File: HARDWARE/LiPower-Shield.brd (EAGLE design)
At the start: 59.7 x 53.3 mm, 51 parts, among them U1 MAX17043G+U, U2 TPS61200, U3 MCP73831, U4 ARDUINO_R3_SHIELD, X1 USBSMD

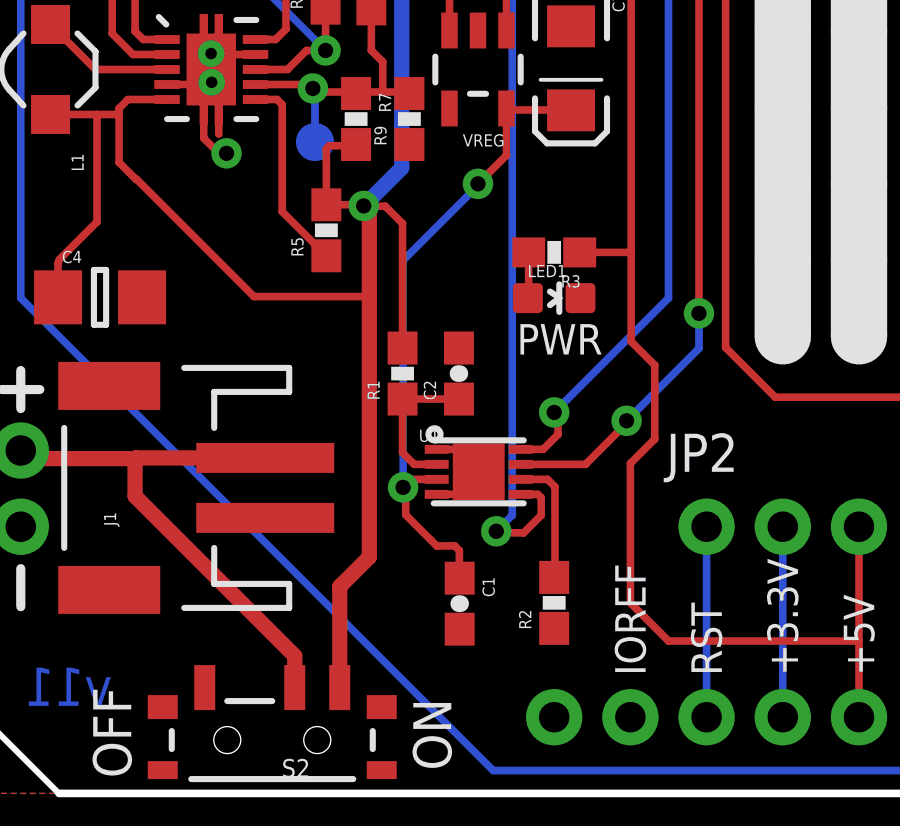
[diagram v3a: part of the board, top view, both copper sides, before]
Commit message: Added test point, Lines around Sch parts and Prod Att
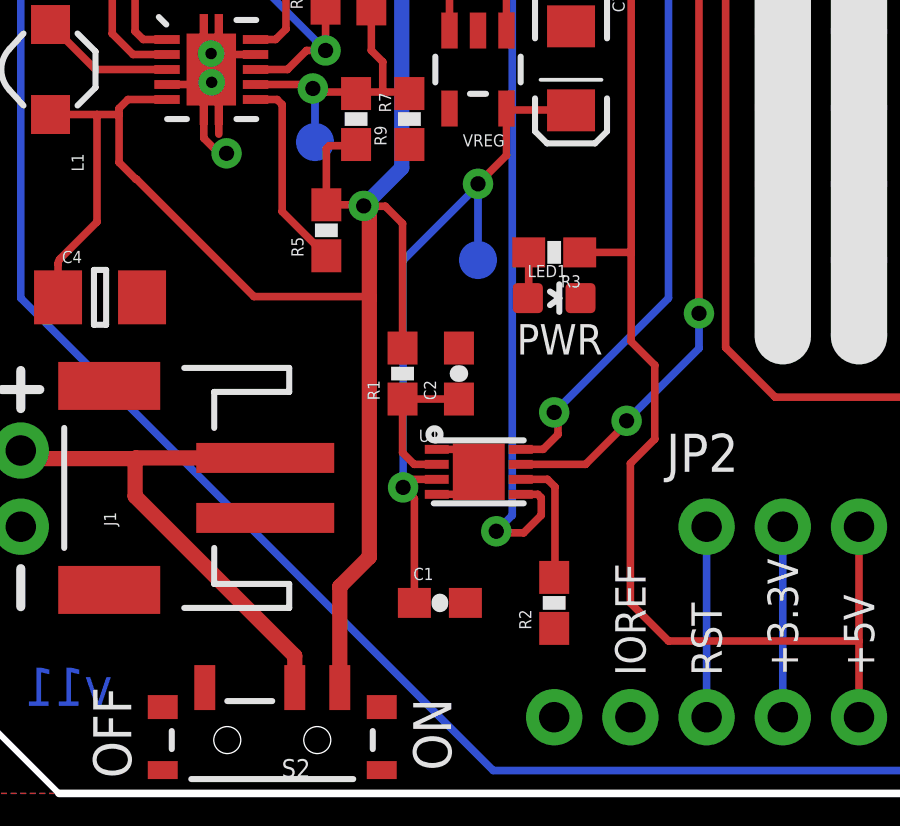
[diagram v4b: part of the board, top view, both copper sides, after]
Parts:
- removed U$2, U$3: (no value), SparkFun-Electromechanical:STAND-OFF-TIGHT
- added JP10, JP9: STAND-OFFTIGHT, SparkFun:STAND-OFF-TIGHT
- added TP2: TEST-POINT3X5, SparkFun-Passives:PAD.03X.05
- C7: device SparkFun:EIA3216 -> SparkFun-Capacitors:EIA3216
- U3, VREG: device SparkFun:SOT23-5 -> SparkFun-PowerIC:SOT23-5
- moved C1 0.66 mm to (15.2, 6.35), turned to 0 degrees
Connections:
- net 3.3V: now also TP2.P$1
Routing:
- net 3.3V: track 21.7 -> 24.5 mm
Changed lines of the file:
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@@
 <layer number="29" name="tStop" color="7" fill="3" visible="no" active="yes"/>
 <layer number="30" name="bStop" color="7" fill="6" visible="no" active="yes"/>
-<layer number="31" name="tCream" color="7" fill="4" visible="no" active="yes"/>
+<layer number="31" name="tCream" color="7" fill="4" visible="yes" active="yes"/>
 <layer number="32" name="bCream" color="7" fill="5" visible="no" active="yes"/>
 <layer number="33" name="tFinish" color="6" fill="3" visible="no" active="yes"/>
@@
 <element name="U4" library="SparkFun-Boards" package="UNO_R3_SHIELD" value="ARDUINO_R3_SHIELD" x="0" y="53.34" rot="R270"/>
 <element name="U1" library="SparkFun" package="TDFN-8" value="MAX17043G+U" x="16.5354" y="10.7188"/>
-<element name="C1" library="SparkFun-Capacitors" package="0603-CAP" value="10nF" x="15.9004" y="6.3246" rot="R270">
-<attribute name="PROD_ID" value="CAP-00867" x="15.9004" y="6.3246" size="1.778" layer="27" rot="R270" display="off"/>
-<attribute name="VALUE" value="10nF" x="15.9004" y="6.3246" size="1.778" layer="27" rot="R270" display="off"/>
-</element>
-<element name="U3" library="SparkFun" package="SOT23-5" value="MCP73831" x="13.97" y="38.1" rot="R90"/>
+<element name="C1" library="SparkFun-Capacitors" package="0603-CAP" value="10nF" x="15.24" y="6.35">
+<attribute name="PROD_ID" value="CAP-00867" x="15.24" y="6.35" size="1.778" layer="27" display="off"/>
+<attribute name="VALUE" value="10nF" x="15.24" y="6.35" size="1.778" layer="27" display="off"/>
+</element>
+<element name="U3" library="SparkFun-PowerIC" package="SOT23-5" value="MCP73831" x="13.97" y="38.1" rot="R90">
+<attribute name="PROD_ID" value="IC-09995" x="13.97" y="38.1" size="1.778" layer="27" rot="R90" display="off"/>
+</element>
 <element name="X1" library="SparkFun-Connectors" package="USB-MINIB" value="USBSMD" x="5.08" y="38.1">
 <attribute name="PROD_ID" value="CONN-08193" x="5.08" y="38.1" size="1.778" layer="27" display="off"/>
@@
 </element>
 <element name="JP4" library="SparkFun-Connectors" package="1X02" value="M02PTH" x="5.953759375" y="45.72" rot="R180"/>
-<element name="VREG" library="SparkFun" package="SOT23-5" value="MIC5205-3.3V" x="16.51" y="24.13" rot="R180"/>
-<element name="C7" library="SparkFun" package="EIA3216" value="10uF" x="19.611340625" y="24.1681" rot="R270"/>
+<element name="VREG" library="SparkFun-PowerIC" package="SOT23-5" value="MIC5205-3.3V" x="16.51" y="24.13" rot="R180">
+<attribute name="PROD_ID" value="VREG-00822" x="16.51" y="24.13" size="1.778" layer="27" rot="R180" display="off"/>
+</element>
+<element name="C7" library="SparkFun-Capacitors" package="EIA3216" value="10uF" x="19.611340625" y="24.1681" rot="R270">
+<attribute name="PROD_ID" value="CAP-00811" x="19.611340625" y="24.1681" size="1.778" layer="27" rot="R270" display="off"/>
+<attribute name="VALUE" value="10uF" x="19.611340625" y="24.1681" size="1.778" layer="27" rot="R270" display="off"/>
+</element>
 <element name="JP1" library="SparkFun" package="1X02_NO_SILK" value="" x="1.27" y="8.89" rot="R90"/>
 <element name="SJ1" library="SparkFun" package="SJ_2S-TRACE" value="SOLDERJUMPERTRACE" x="19.05" y="30.48" rot="MR90"/>
@@
 <element name="LOGO1" library="SparkFun-Aesthetics" package="OSHW-LOGO-S" value="OSHW-LOGOS" x="2.092959375" y="30.5562"/>
 <element name="LOGO2" library="SparkFun-Aesthetics" package="SFE_LOGO_NAME_FLAME_.2" value="SFE_LOGO_NAME_FLAME.2_INCH" x="2.54" y="12.446" rot="MR90"/>
-<element name="U$2" library="SparkFun-Electromechanical" package="STAND-OFF-TIGHT" value="" x="57.15" y="6.35"/>
-<element name="U$3" library="SparkFun-Electromechanical" package="STAND-OFF-TIGHT" value="" x="5.08" y="50.8"/>
 <element name="SJ3" library="SparkFun-Passives" package="PAD-JUMPER-3-2OF3_NC_BY_TRACE_YES_SILK_FULL_BOX" value="SDA" x="12.7" y="47.752" rot="MR270"/>
 <element name="SJ4" library="SparkFun-Passives" package="PAD-JUMPER-3-2OF3_NC_BY_TRACE_YES_SILK_FULL_BOX" value="SCL" x="10.16" y="47.879" rot="MR270"/>
@@
 <attribute name="PROD_ID" value="RES-10054" x="12.446" y="22.479" size="1.778" layer="27" font="vector" ratio="15" rot="R270" display="off"/>
 </element>
+<element name="TP2" library="SparkFun-Passives" package="PAD.03X.05" value="TEST-POINT3X5" x="16.51" y="17.78" rot="MR0"/>
+<element name="JP9" library="SparkFun" package="STAND-OFF-TIGHT" value="STAND-OFFTIGHT" x="5.08" y="50.8"/>
+<element name="JP10" library="SparkFun" package="STAND-OFF-TIGHT" value="STAND-OFFTIGHT" x="57.15" y="6.35"/>
 </elements>
 <signals>
@@
 <via x="14.013178125" y="10.2006375" extent="1-16" drill="0.508"/>
 <via x="16.51" y="20.32" extent="1-16" drill="0.508"/>
-<wire x1="15.8886" y1="7.1628" x2="15.9004" y2="7.1746" width="0.254" layer="1"/>
 <wire x1="14.013178125" y1="10.2006375" x2="14.013178125" y2="17.764759375" width="0.254" layer="16"/>
 <wire x1="17.5599" y1="22.73" x2="17.6107" y2="22.7808" width="0.254" layer="1"/>
@@
 <wire x1="16.51" y1="20.32" x2="16.51" y2="20.26158125" width="0.254" layer="16"/>
 <wire x1="16.51" y1="20.26158125" x2="14.013178125" y2="17.764759375" width="0.254" layer="16"/>
-<wire x1="15.8886" y1="7.1628" x2="15.8886" y2="8.09661875" width="0.254" layer="1"/>
-<wire x1="15.8886" y1="8.09661875" x2="15.7353" y2="8.24991875" width="0.254" layer="1"/>
-<wire x1="15.7353" y1="8.24991875" x2="15.133321875" y2="8.24991875" width="0.254" layer="1"/>
-<wire x1="15.133321875" y1="8.24991875" x2="14.10208125" y2="9.281159375" width="0.254" layer="1"/>
-<wire x1="14.10208125" y1="9.281159375" x2="14.10208125" y2="10.111734375" width="0.254" layer="1"/>
-<wire x1="14.10208125" y1="10.111734375" x2="14.013178125" y2="10.2006375" width="0.254" layer="1"/>
 <wire x1="15.1354" y1="10.4688" x2="14.281340625" y2="10.4688" width="0.254" layer="1"/>
 <wire x1="14.281340625" y1="10.4688" x2="14.013178125" y2="10.2006375" width="0.254" layer="1"/>
+<contactref element="TP2" pad="P$1"/>
+<wire x1="14.10208125" y1="6.63791875" x2="14.39" y2="6.35" width="0.254" layer="1"/>
+<wire x1="16.51" y1="17.78" x2="16.51" y2="20.32" width="0.254" layer="16"/>
+<wire x1="14.013178125" y1="10.2006375" x2="14.39" y2="9.823815625" width="0.254" layer="1"/>
+<wire x1="14.39" y1="9.823815625" x2="14.39" y2="6.35" width="0.254" layer="1"/>
 </signal>
 <signal name="VBATT">
@@
 </signal>
 </signals>
+<errors>
+</errors>
 </board>
 </drawing>

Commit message: Reduced paste on IC's
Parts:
- U1: device SparkFun:TDFN-8 -> SparkFun-PowerIC:TDFN-8
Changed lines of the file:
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@@
 <layer number="29" name="tStop" color="7" fill="3" visible="no" active="yes"/>
 <layer number="30" name="bStop" color="7" fill="6" visible="no" active="yes"/>
-<layer number="31" name="tCream" color="7" fill="4" visible="yes" active="yes"/>
+<layer number="31" name="tCream" color="7" fill="4" visible="no" active="yes"/>
 <layer number="32" name="bCream" color="7" fill="5" visible="no" active="yes"/>
 <layer number="33" name="tFinish" color="6" fill="3" visible="no" active="yes"/>
@@
 <layer number="47" name="Measures" color="7" fill="1" visible="no" active="yes"/>
 <layer number="48" name="Document" color="7" fill="1" visible="no" active="yes"/>
-<layer number="49" name="Reference" color="7" fill="1" visible="no" active="yes"/>
+<layer number="49" name="Reference" color="7" fill="1" visible="yes" active="yes"/>
 <layer number="50" name="dxf" color="7" fill="1" visible="no" active="yes"/>
 <layer number="51" name="tDocu" color="6" fill="1" visible="yes" active="yes"/>
@@
 <elements>
 <element name="U4" library="SparkFun-Boards" package="UNO_R3_SHIELD" value="ARDUINO_R3_SHIELD" x="0" y="53.34" rot="R270"/>
-<element name="U1" library="SparkFun" package="TDFN-8" value="MAX17043G+U" x="16.5354" y="10.7188"/>
+<element name="U1" library="SparkFun-PowerIC" package="TDFN-8" value="MAX17043G+U" x="16.5354" y="10.7188">
+<attribute name="PROD-ID" value="IC-10399" x="16.5354" y="10.7188" size="1.778" layer="27" display="off"/>
+</element>
 <element name="C1" library="SparkFun-Capacitors" package="0603-CAP" value="10nF" x="15.24" y="6.35">
 <attribute name="PROD_ID" value="CAP-00867" x="15.24" y="6.35" size="1.778" layer="27" display="off"/>
@@
 </signal>
 </signals>
-<errors>
-</errors>
 </board>
 </drawing>

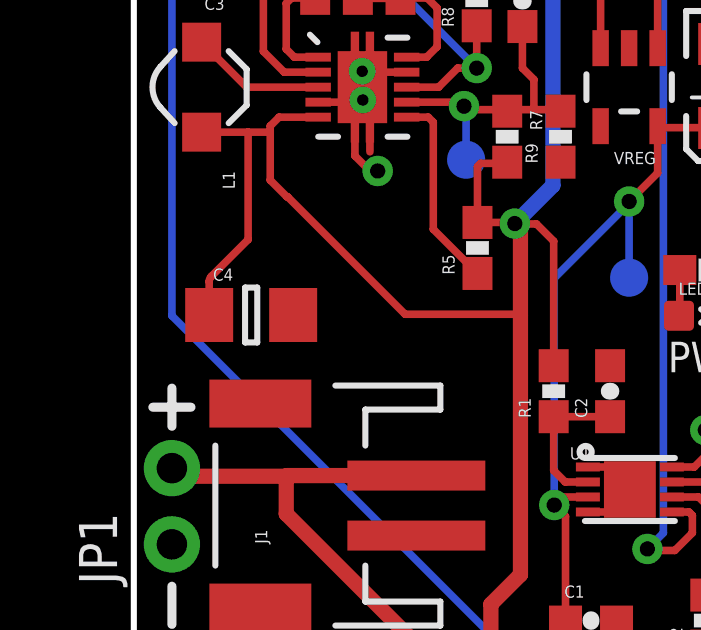
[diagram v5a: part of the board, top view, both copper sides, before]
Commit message: Added prod id's for nduc/caps
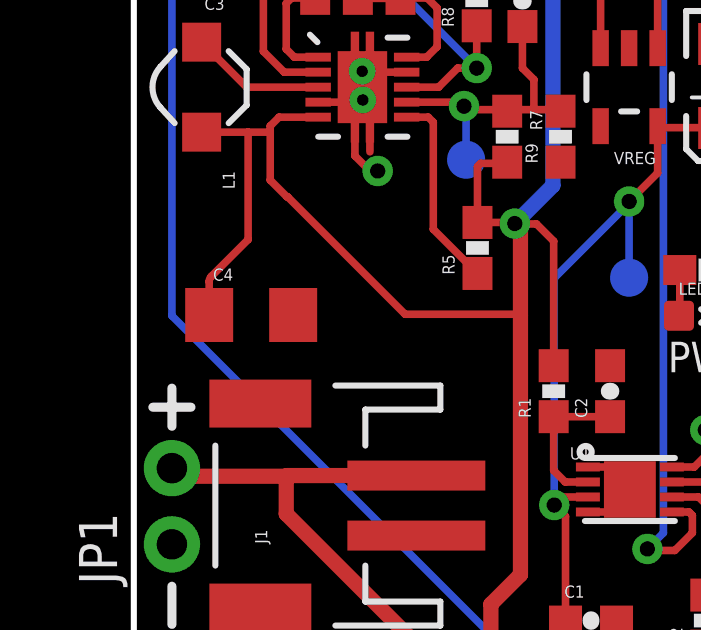
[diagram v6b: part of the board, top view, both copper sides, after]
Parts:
- C3: device CH_passive:0805 -> SparkFun-Capacitors:0805
- C4: device CH_passive:1206 -> SparkFun-Capacitors:1206
- L1: device SparkFun:CDRH2D09 -> SparkFun-Passives:INDUCTOR_4.7UH
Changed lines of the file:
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@@
 <layer number="29" name="tStop" color="7" fill="3" visible="no" active="yes"/>
 <layer number="30" name="bStop" color="7" fill="6" visible="no" active="yes"/>
-<layer number="31" name="tCream" color="7" fill="4" visible="no" active="yes"/>
+<layer number="31" name="tCream" color="7" fill="4" visible="yes" active="yes"/>
 <layer number="32" name="bCream" color="7" fill="5" visible="no" active="yes"/>
 <layer number="33" name="tFinish" color="6" fill="3" visible="no" active="yes"/>
@@
 <layer number="47" name="Measures" color="7" fill="1" visible="no" active="yes"/>
 <layer number="48" name="Document" color="7" fill="1" visible="no" active="yes"/>
-<layer number="49" name="Reference" color="7" fill="1" visible="yes" active="yes"/>
+<layer number="49" name="Reference" color="7" fill="1" visible="no" active="yes"/>
 <layer number="50" name="dxf" color="7" fill="1" visible="no" active="yes"/>
 <layer number="51" name="tDocu" color="6" fill="1" visible="yes" active="yes"/>
@@
 <attribute name="VALUE" value="330" x="19.05" y="18.034" size="1.778" layer="27" rot="R180" display="off"/>
 </element>
-<element name="C3" library="CH_passive" package="0805" value="22uF" x="2.2606" y="27.94" rot="R180"/>
+<element name="C3" library="SparkFun-Capacitors" package="0805" value="22uF" x="2.2606" y="27.94" rot="R180">
+<attribute name="PROD_ID" value="CAP-08402" x="2.2606" y="27.94" size="1.778" layer="27" rot="R180" display="off"/>
+<attribute name="VALUE" value="22uF" x="2.2606" y="27.94" size="1.778" layer="27" rot="R180" display="off"/>
+</element>
 <element name="U2" library="SparkFun-PowerIC" package="QFN-10_PAD" value="TPS61200" x="7.62" y="24.13" rot="R270">
 <attribute name="PROD_ID" value="IC-10035" x="7.62" y="24.13" size="1.778" layer="27" rot="R270" display="off"/>
@@
 <attribute name="VALUE" value="2.0M" x="7.4676" y="27.94" size="1.778" layer="27" rot="R90" display="off"/>
 </element>
-<element name="C4" library="CH_passive" package="1206" value="10uF" x="3.9116" y="16.5354"/>
-<element name="L1" library="SparkFun" package="CDRH2D09" value="4.7uH, 1.2A" x="2.2606" y="24.13" rot="R270"/>
+<element name="C4" library="SparkFun-Capacitors" package="1206" value="10uF" x="3.9116" y="16.5354">
+<attribute name="PROD_ID" value="CAP-10057" x="3.9116" y="16.5354" size="1.778" layer="27" display="off"/>
+<attribute name="VALUE" value="10uF" x="3.9116" y="16.5354" size="1.778" layer="27" display="off"/>
+</element>
+<element name="L1" library="SparkFun-Passives" package="INDUCTOR_4.7UH" value="4.7uH, 1.2A" x="2.2606" y="24.13" rot="R270">
+<attribute name="PROD_ID" value="NDUC-10146" x="2.2606" y="24.13" size="1.778" layer="27" rot="R270" display="off"/>
+</element>
 <element name="R5" library="SparkFun-Resistors" package="0603-RES" value="10k" x="11.4554" y="18.7706" rot="R90">
 <attribute name="PROD_ID" value="RES-00824" x="11.4554" y="18.7706" size="1.778" layer="27" rot="R90" display="off"/>
